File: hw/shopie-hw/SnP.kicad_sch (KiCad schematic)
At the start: 15 parts, among them U5 HAKRC_Blehli32_ESC40A

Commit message: Add custom footprint for BMS board, Add TMF8801 footprint
- Created custom footprint for the BMS board
- Imported TMF8801 sensor footprint
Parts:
- U?: footprint BMP388:PQFN50P200X200X80-10N -> ShopieLibrary:BMP388
- U?: footprint TMF8801-1BM_AMS -> ShopieLibrary:TMF8801-1BM_AMS
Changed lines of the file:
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@@
 			)
 		)
-		(property "Footprint" "BMP388:PQFN50P200X200X80-10N"
+		(property "Footprint" "ShopieLibrary:BMP388"
 			(at 120.65 45.72 0)
 			(effects
@@
 		(on_board yes)
 		(dnp no)
-		(property "Reference" "#PWR?"
+		(property "Reference" "#PWR0108"
 			(at 158.75 59.69 0)
 			(effects
@@
 			(project "shopie-hw"
 				(path "/e9514a67-47f8-4b41-a728-bdf26e012bf7/d28d3f47-b0c1-4fbb-bdab-a8b85a0388d0"
-					(reference "#PWR?")
+					(reference "#PWR0108")
 					(unit 1)
 				)
@@
 		(on_board yes)
 		(dnp no)
-		(property "Reference" "#PWR?"
+		(property "Reference" "#PWR0101"
 			(at 50.8 24.13 0)
 			(effects
@@
 			(project "shopie-hw"
 				(path "/e9514a67-47f8-4b41-a728-bdf26e012bf7/d28d3f47-b0c1-4fbb-bdab-a8b85a0388d0"
-					(reference "#PWR?")
+					(reference "#PWR0101")
 					(unit 1)
 				)
@@
 		(on_board yes)
 		(dnp no)
-		(property "Reference" "#PWR?"
+		(property "Reference" "#PWR0105"
 			(at 36.83 39.37 0)
 			(effects
@@
 			(project "shopie-hw"
 				(path "/e9514a67-47f8-4b41-a728-bdf26e012bf7/d28d3f47-b0c1-4fbb-bdab-a8b85a0388d0"
-					(reference "#PWR?")
+					(reference "#PWR0105")
 					(unit 1)
 				)
@@
 		(on_board yes)
 		(dnp no)
-		(property "Reference" "#PWR?"
+		(property "Reference" "#PWR0107"
 			(at 158.75 33.02 0)
 			(effects
@@
 			(project "shopie-hw"
 				(path "/e9514a67-47f8-4b41-a728-bdf26e012bf7/d28d3f47-b0c1-4fbb-bdab-a8b85a0388d0"
-					(reference "#PWR?")
+					(reference "#PWR0107")
 					(unit 1)
 				)
@@
 		(on_board yes)
 		(dnp no)
-		(property "Reference" "#PWR?"
+		(property "Reference" "#PWR0111"
 			(at 196.85 58.42 0)
 			(effects
@@
 			(project "shopie-hw"
 				(path "/e9514a67-47f8-4b41-a728-bdf26e012bf7/d28d3f47-b0c1-4fbb-bdab-a8b85a0388d0"
-					(reference "#PWR?")
+					(reference "#PWR0111")
 					(unit 1)
 				)
@@
 		(on_board yes)
 		(dnp no)
-		(property "Reference" "#PWR?"
+		(property "Reference" "#PWR0109"
 			(at 182.88 30.48 0)
 			(effects
@@
 			(project "shopie-hw"
 				(path "/e9514a67-47f8-4b41-a728-bdf26e012bf7/d28d3f47-b0c1-4fbb-bdab-a8b85a0388d0"
-					(reference "#PWR?")
+					(reference "#PWR0109")
 					(unit 1)
 				)
@@
 		(on_board yes)
 		(dnp no)
-		(property "Reference" "#PWR?"
+		(property "Reference" "#PWR0114"
 			(at 275.59 34.29 0)
 			(effects
@@
 			(project "shopie-hw"
 				(path "/e9514a67-47f8-4b41-a728-bdf26e012bf7/d28d3f47-b0c1-4fbb-bdab-a8b85a0388d0"
-					(reference "#PWR?")
+					(reference "#PWR0114")
 					(unit 1)
 				)
@@
 		(on_board yes)
 		(dnp no)
-		(property "Reference" "#PWR?"
+		(property "Reference" "#PWR0104"
 			(at 53.34 73.66 0)
 			(effects
@@
 			(project "shopie-hw"
 				(path "/e9514a67-47f8-4b41-a728-bdf26e012bf7/d28d3f47-b0c1-4fbb-bdab-a8b85a0388d0"
-					(reference "#PWR?")
+					(reference "#PWR0104")
 					(unit 1)
 				)
@@
 		(on_board yes)
 		(dnp no)
-		(property "Reference" "#PWR?"
+		(property "Reference" "#PWR0113"
 			(at 270.51 41.91 0)
 			(effects
@@
 			(project "shopie-hw"
 				(path "/e9514a67-47f8-4b41-a728-bdf26e012bf7/d28d3f47-b0c1-4fbb-bdab-a8b85a0388d0"
-					(reference "#PWR?")
+					(reference "#PWR0113")
 					(unit 1)
 				)
@@
 			)
 		)
-		(property "Footprint" "TMF8801-1BM_AMS"
+		(property "Footprint" "ShopieLibrary:TMF8801-1BM_AMS"
 			(at 201.93 31.75 0)
 			(effects
@@
 		(on_board yes)
 		(dnp no)
-		(property "Reference" "#PWR?"
+		(property "Reference" "#PWR0115"
 			(at 255.27 29.21 0)
 			(effects
@@
 			(project "shopie-hw"
 				(path "/e9514a67-47f8-4b41-a728-bdf26e012bf7/d28d3f47-b0c1-4fbb-bdab-a8b85a0388d0"
-					(reference "#PWR?")
+					(reference "#PWR0115")
 					(unit 1)
 				)
@@
 		(dnp no)
 		(fields_autoplaced yes)
-		(property "Reference" "#PWR?"
+		(property "Reference" "#PWR0103"
 			(at 29.21 50.8 0)
 			(effects
@@
 			(project "shopie-hw"
 				(path "/e9514a67-47f8-4b41-a728-bdf26e012bf7/d28d3f47-b0c1-4fbb-bdab-a8b85a0388d0"
-					(reference "#PWR?")
+					(reference "#PWR0103")
 					(unit 1)
 				)
@@
 		(dnp no)
 		(fields_autoplaced yes)
-		(property "Reference" "#PWR?"
+		(property "Reference" "#PWR0110"
 			(at 184.15 50.8 0)
 			(effects
@@
 			(project "shopie-hw"
 				(path "/e9514a67-47f8-4b41-a728-bdf26e012bf7/d28d3f47-b0c1-4fbb-bdab-a8b85a0388d0"
-					(reference "#PWR?")
+					(reference "#PWR0110")
 					(unit 1)
 				)
@@
 		(on_board yes)
 		(dnp no)
-		(property "Reference" "#PWR?"
+		(property "Reference" "#PWR0102"
 			(at 69.85 39.37 0)
 			(effects
@@
 			(project "shopie-hw"
 				(path "/e9514a67-47f8-4b41-a728-bdf26e012bf7/d28d3f47-b0c1-4fbb-bdab-a8b85a0388d0"
-					(reference "#PWR?")
+					(reference "#PWR0102")
 					(unit 1)
 				)
@@
 		(on_board yes)
 		(dnp no)
-		(property "Reference" "#PWR?"
+		(property "Reference" "#PWR0106"
 			(at 55.88 24.13 0)
 			(effects
@@
 			(project "shopie-hw"
 				(path "/e9514a67-47f8-4b41-a728-bdf26e012bf7/d28d3f47-b0c1-4fbb-bdab-a8b85a0388d0"
-					(reference "#PWR?")
+					(reference "#PWR0106")
 					(unit 1)
 				)
@@
 		(on_board yes)
 		(dnp no)
-		(property "Reference" "#PWR?"
+		(property "Reference" "#PWR0112"
 			(at 247.65 52.07 0)
 			(effects
@@
 			(project "shopie-hw"
 				(path "/e9514a67-47f8-4b41-a728-bdf26e012bf7/d28d3f47-b0c1-4fbb-bdab-a8b85a0388d0"
-					(reference "#PWR?")
-					(unit 1)
-				)
+					(reference "#PWR0112")
+					(unit 1)
+				)

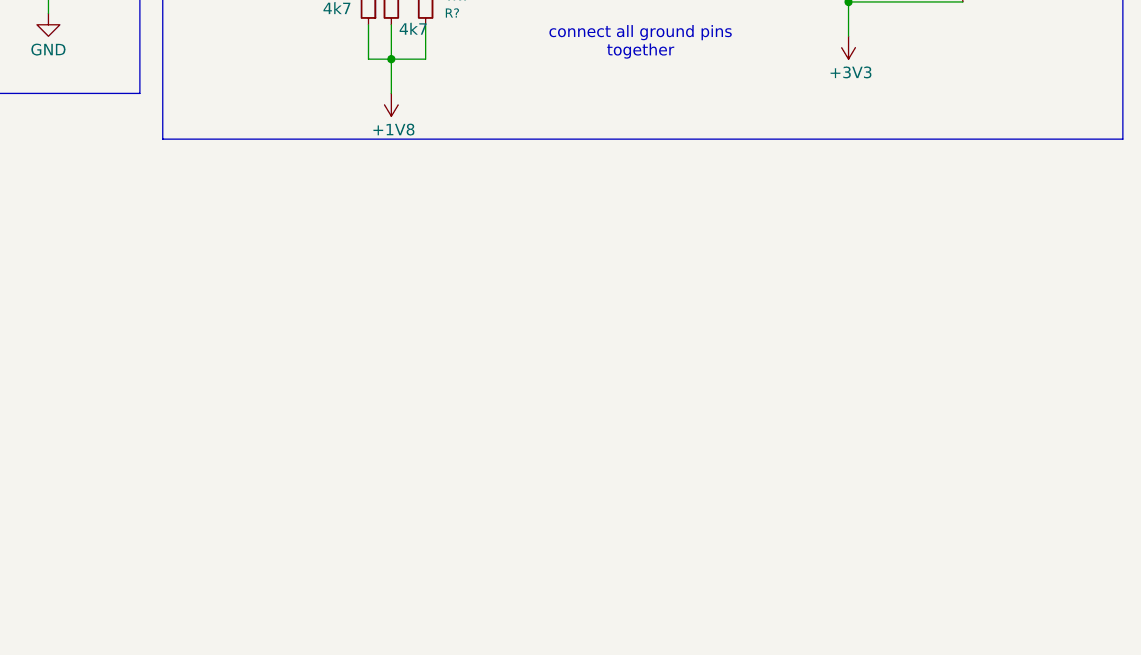
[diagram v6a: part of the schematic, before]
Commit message: Update Main Power Block
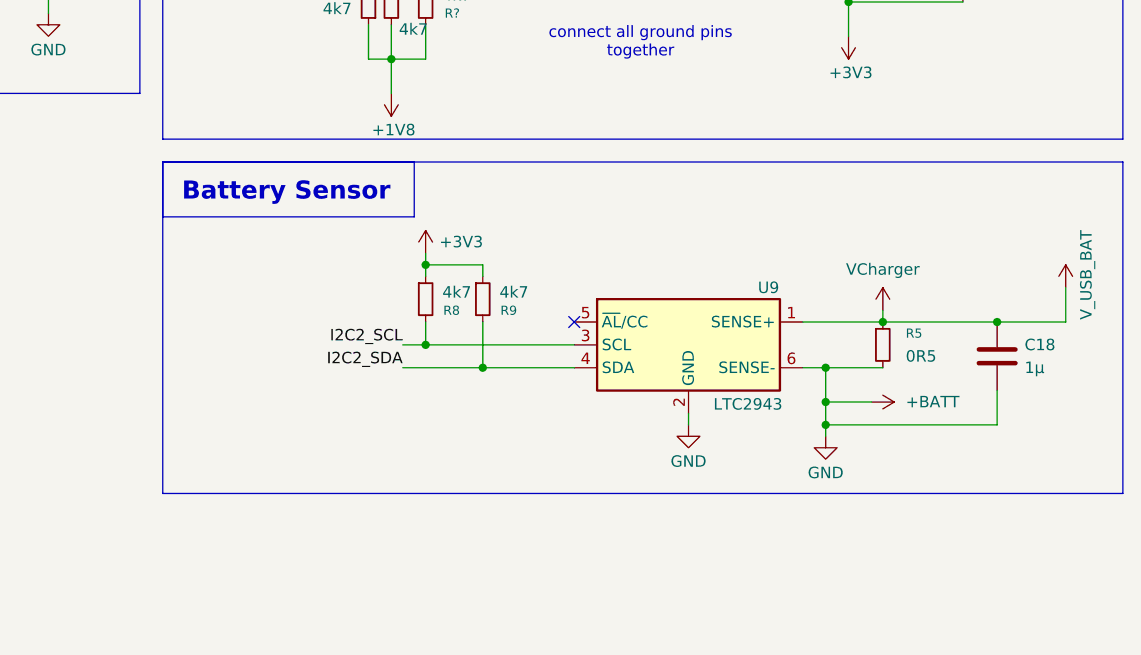
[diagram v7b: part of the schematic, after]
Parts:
- added C18: 1µ, symbol Device:C
- added R5: 0R5, symbol Device:R_Small
- added R8, R9: 4k7, symbol Device:R_Small
- added U9: LTC2943, Package_DFN_QFN:DFN-6-1EP_3x2mm_P0.5mm_EP1.65x1.35mm, symbol Battery_Management:LTC2942
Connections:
- net V_USB_BAT is gone; now on net VCharger: U5. (M1P1)
- net +3V3: now also R8.1, R9.1
- net VCharger: now reaches U5. (M1P1)
- net VCharger: now also C18.1, R5.1, U9.1 (SENSE+)
- net GND renamed +BATT
- net +BATT: now also C18.2, R5.2, U9.2 (GND), U9.6 (SENSE-)
- new net I2C2_SCL: R8.2, U9.3 (SCL)
- new net I2C2_SDA: R9.2, U9.4 (SDA)
- no-connect marks 17 -> 18
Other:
- note added: "Battery Sensor"

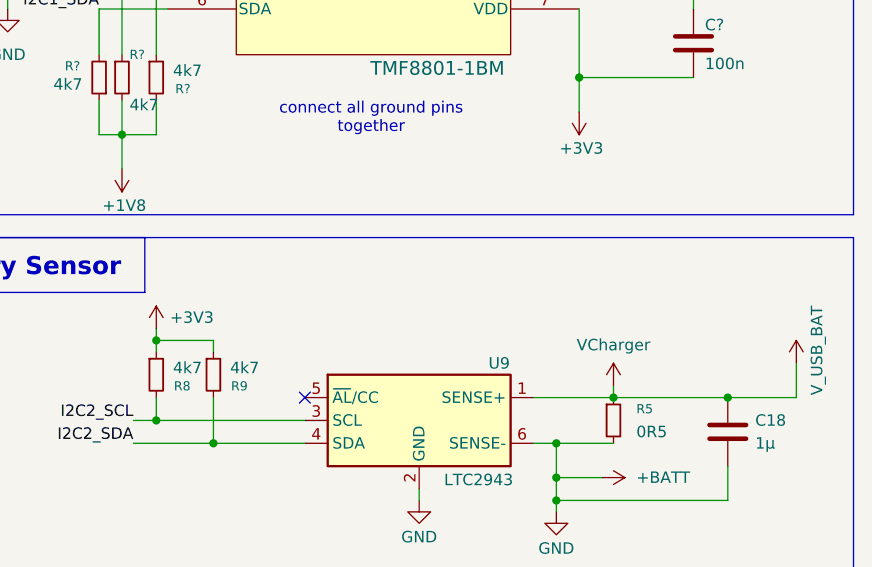
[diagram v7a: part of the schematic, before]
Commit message: Add BSC016N06NS Symbol and Footprint
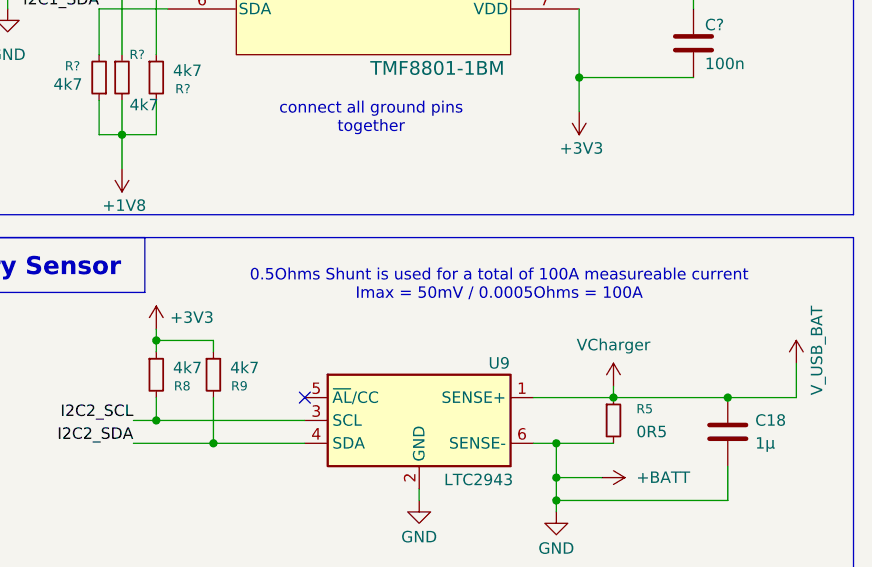
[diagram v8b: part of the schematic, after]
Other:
- note added: "0.5Ohms Shunt is used for a total of 100A measureable current Imax = 50mV / 0.0005Ohms = 100A"
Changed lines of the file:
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@@
+		)
+	)
+	(text "0.5Ohms Shunt is used for a total of 100A measureable current\nImax = 50mV / 0.0005Ohms = 100A"
+		(exclude_from_sim no)
+		(at 238.76 75.184 0)
+		(effects
+			(font
+				(size 1.27 1.27)
+			)
 		)
 	)
